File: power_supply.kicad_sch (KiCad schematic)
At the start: 21 parts, among them J1 USB_C_Receptacle_USB2.0_16P, J2 USB_C_Receptacle_USB2.0_16P

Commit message: fix: fixes schematic errors and some layout errors
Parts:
- U1: MPN TLV74033PDBVR -> TLV78533PDBVR
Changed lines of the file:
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@@
 			)
 		)
-		(property "Datasheet" "https://www.digikey.com.br/pt/products/detail/texas-instruments/TLV74033PDBVR/12642183?s=N4IgTCBcDaICoBkBqB2ALABgMxYAoBEAhJAJRAF0BfIA"
+		(property "Datasheet" "https://www.digikey.com.br/en/products/detail/texas-instruments/TLV78533PDBVR/26812391"
 			(at 139.7 54.61 0)
 			(effects
@@
 			)
 		)
-		(property "MPN" "TLV74033PDBVR"
+		(property "MPN" "TLV78533PDBVR"
 			(at 143.51 58.42 0)
 			(effects

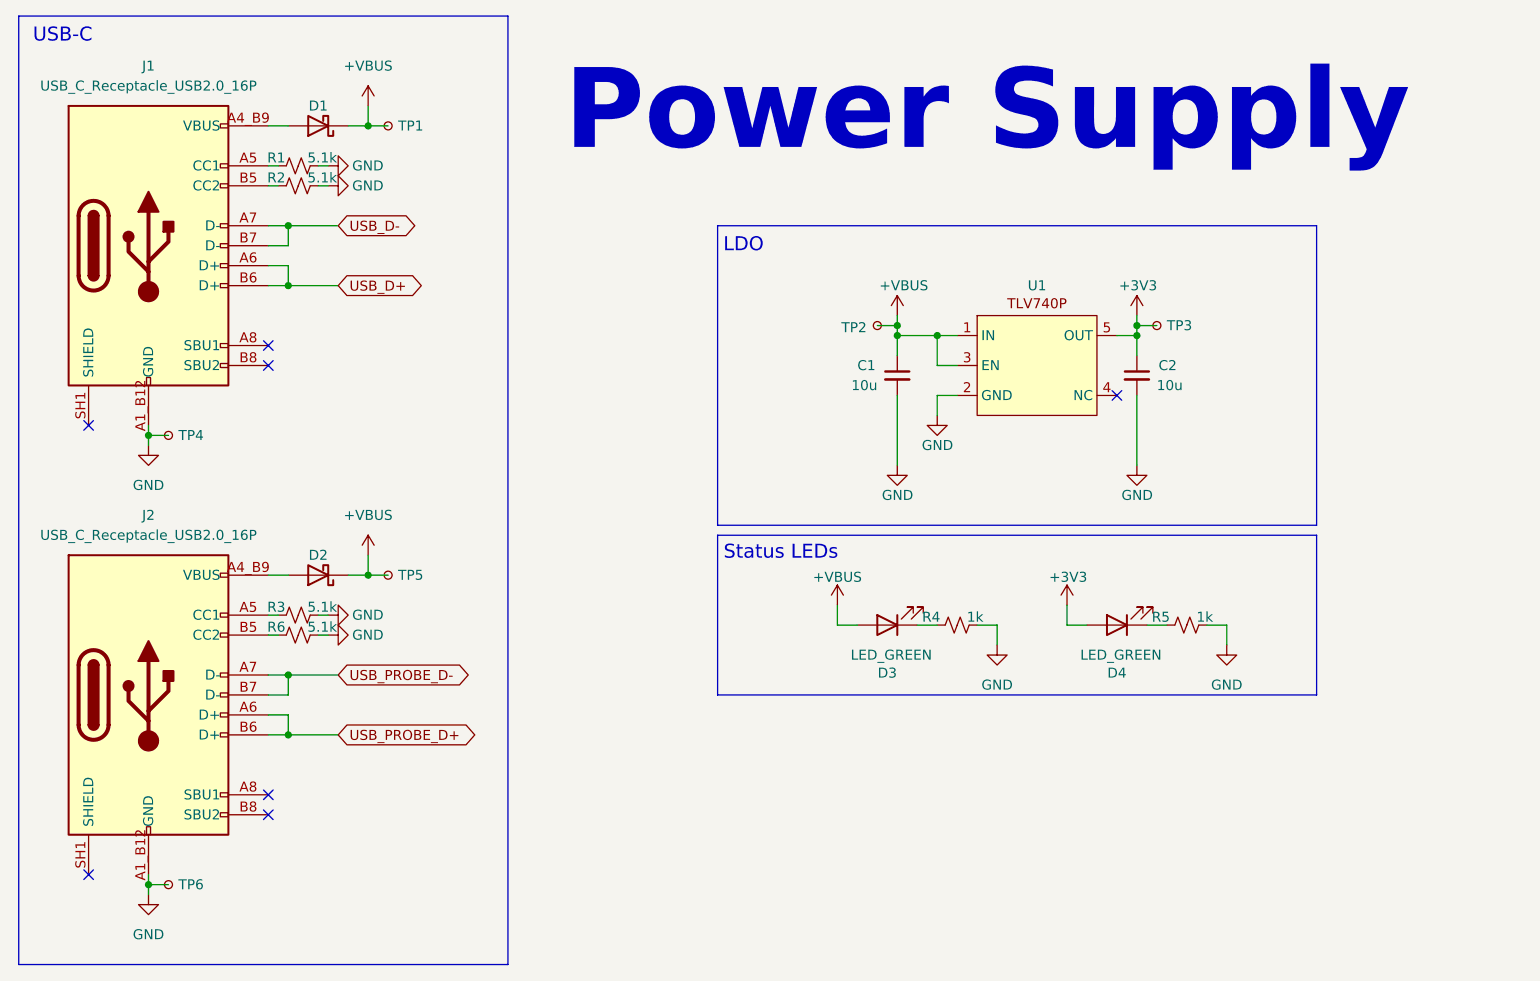
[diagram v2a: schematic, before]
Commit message: refac: changes OR circuit in power supply
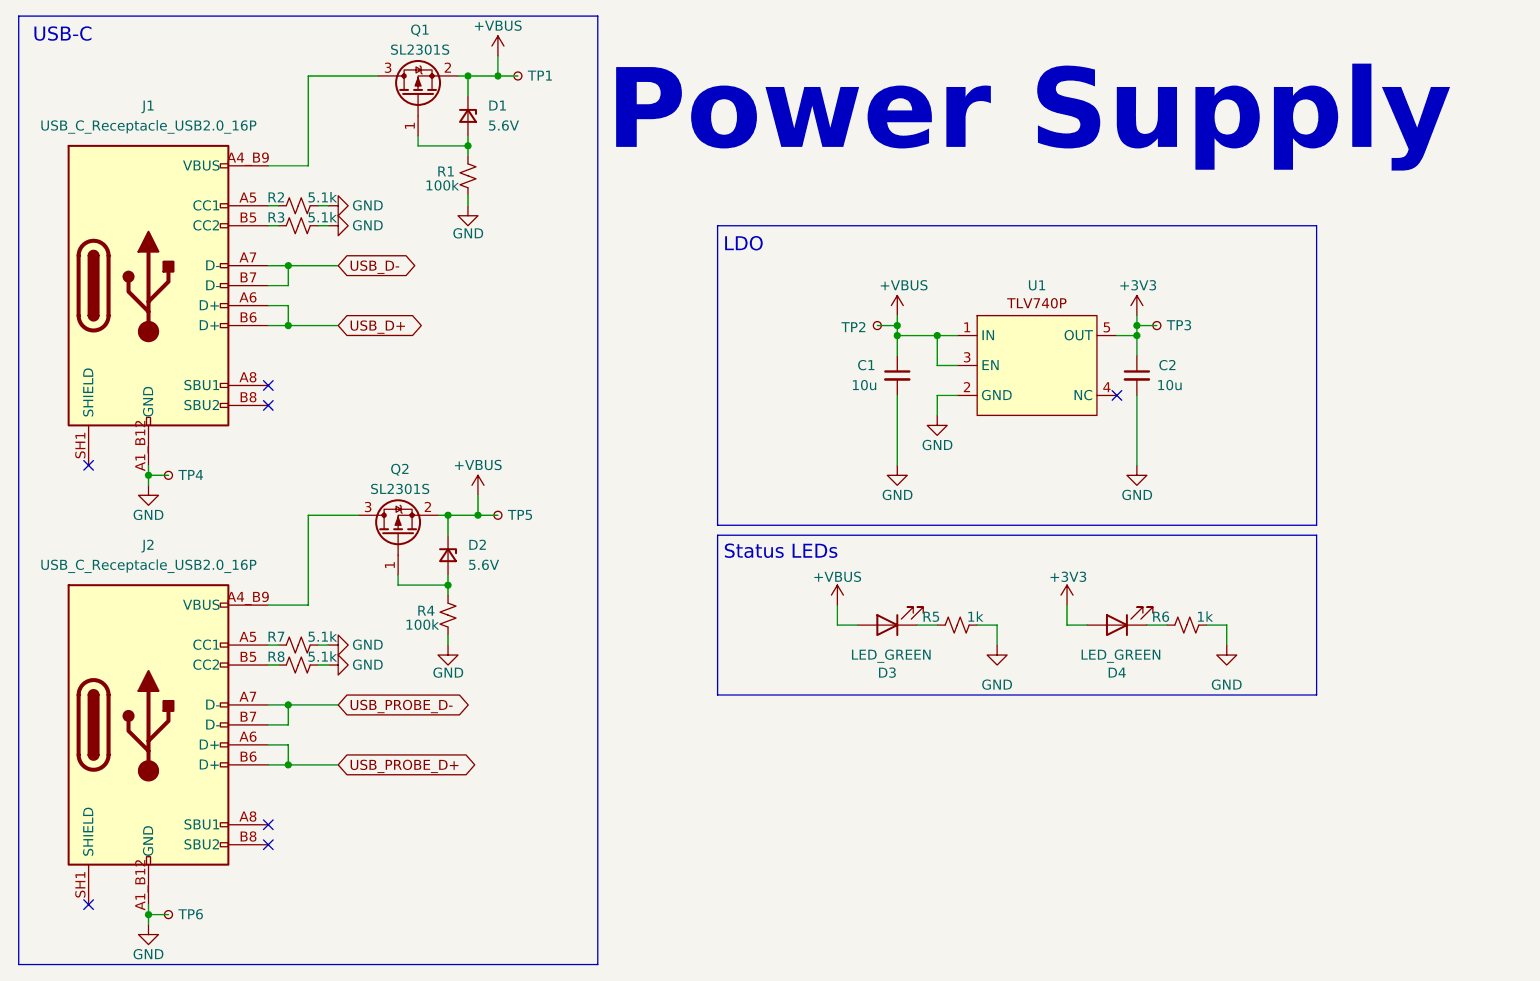
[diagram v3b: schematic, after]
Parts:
- removed D1, D2: D_Schottky, Diode_SMD:D_SOD-123F, symbol Device:D_Schottky
- added D1, D2: 5.6V, Diode_SMD:D_SOD-123F, symbol Device:D_Zener_Small
- added Q1, Q2: SL2301S, Package_TO_SOT_SMD:SOT-23, symbol Transistor_FET:AO3401A
- added R1, R4: 100k, Resistor_SMD:R_0402_1005Metric, symbol Device:R_Small_US
- renumbered R1 to R2, R2 to R3, R4 to R5, R5 to R6, R3 to R7, R6 to R8
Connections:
- net +VBUS: now also D1.1 (K), D2.1 (K), Q1.2 (S), Q2.2 (S)
- net GND: now also R1.1, R4.1
- net at J2.A4_B9 (VBUS), J2.B4_A9 (VBUS): now also Q2.3 (D)
- net at J1.A4_B9 (VBUS), J1.B4_A9 (VBUS): now also Q1.3 (D)
- new net: D2.2 (A), Q2.1 (G), R4.2
- new net: D1.2 (A), Q1.1 (G), R1.2
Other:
- moved on the sheet: J1, J2, R2, R3, R7, R8, TP1, TP4, TP6

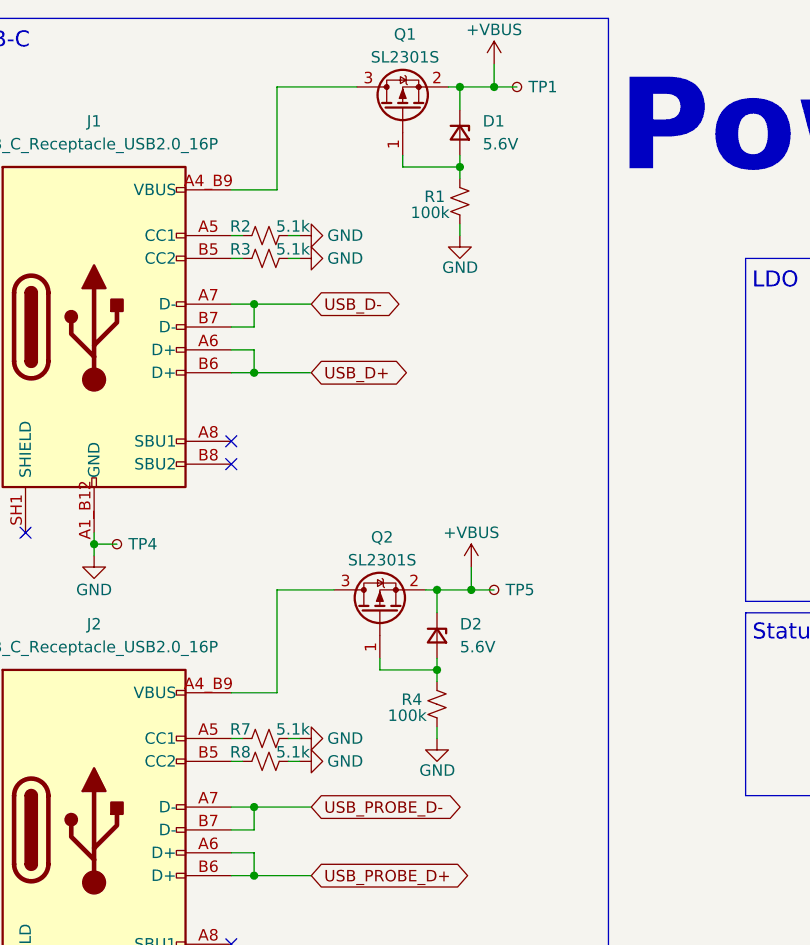
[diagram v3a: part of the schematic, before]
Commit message: feat: adds 4th wire to display, removes remaining sdcard lines
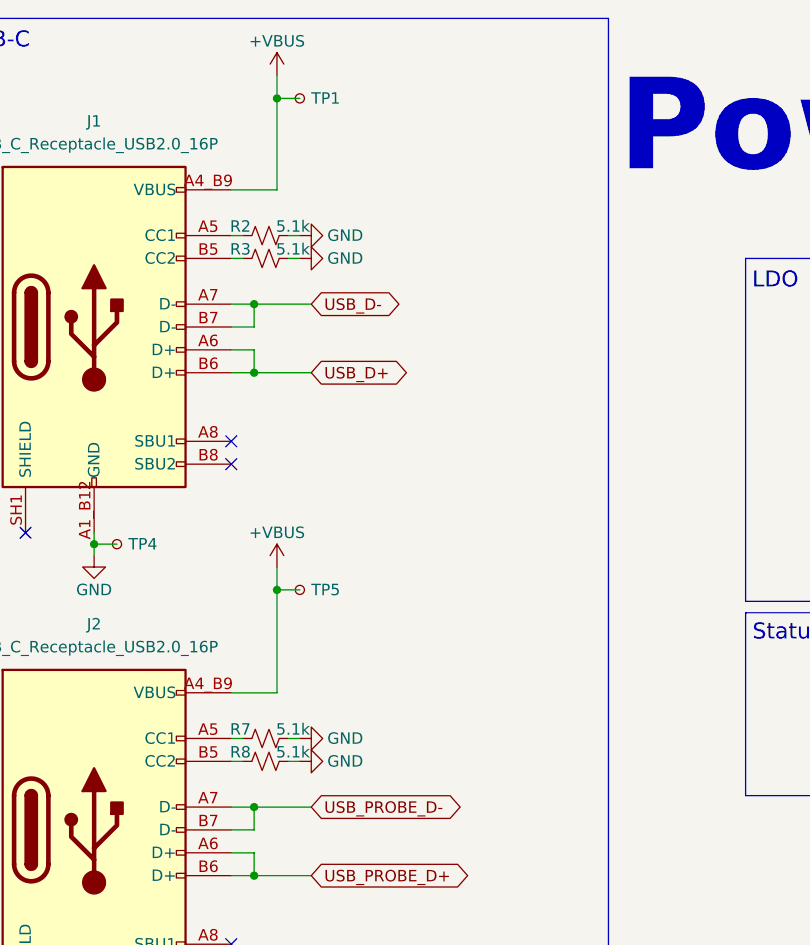
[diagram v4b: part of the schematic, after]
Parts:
- removed D1, D2: 5.6V, Diode_SMD:D_SOD-123F, symbol Device:D_Zener_Small
- removed Q1, Q2: SL2301S, Package_TO_SOT_SMD:SOT-23, symbol Transistor_FET:AO3401A
- removed R1, R4: 100k, Resistor_SMD:R_0402_1005Metric, symbol Device:R_Small_US
- U1: value ~ -> TLV78533PDBVR
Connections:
- net +VBUS: now also J1.A4_B9 (VBUS), J1.B4_A9 (VBUS), J2.A4_B9 (VBUS), J2.B4_A9 (VBUS)
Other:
- moved on the sheet: TP1, TP5
